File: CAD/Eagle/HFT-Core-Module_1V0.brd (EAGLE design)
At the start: 96.5 x 96.5 mm, 392 parts, among them Q0521 ABS07-32.768KHZ, Q0811 ABM03B-32.000MHZ, Q0911 ABM3B-16MHZ-10-R50-1-U, T1201 MMBT2222, T1202 MMBT2222, T1203 MMBT2222, U0111 STM32L4Z_144PIN_SMPS, U0431 PAM2305AAB120, U0601 LM4120IM5-3.0, U0611 MAX5217, U0631 CFPT-141-20MHZ, U0641 OPA354, U0701 Si5338, U0801 SX1276, U0901 AX5243, U0911 PE4259, U0921 PE4259, U0991 PE4259, U1011 MAX5136AGTG+, U1101 MCP3911A0-E-SS, U1121 OPA354, U1131 OPA354, U1141 OPA354, U1201 NHD-C0220BIZ_2X20CHARS, U1301 MPU-9250, U1311 MS5607-02BA03, U1321 SHT31-DIS, U1401 SOLARPANEL_3V3_5MA1_25MM_X_20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, U1402 SPV1040T, U1501 TS5A23166, U1601 PAM2305AAB330, U1701 TS5A23166, U1801 TS5A23166, U1901 TS5A23166, X1261 TTE_EN11-HSM, X2101 SMA_SMT_AMPHENOL-901-143, X2111 SMA_SMT_AMPHENOL-901-143, X2201 CUI SJ1-3535NS, X2211 CUI SJ1-3535NS, X2311 2X20/90_1MM27_HARWIN_M50-3202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, X2312 2X20/90_1MM27_HARWIN_M50-3202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, X2321 2X20/90_1MM27_HARWIN_M50-3202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, X2322 2X20/90_1MM27_HARWIN_M50-3202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, X2331 2X20/90_1MM27_HARWIN_M50-3202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, X2332 2X20/90_1MM27_HARWIN_M50-3202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

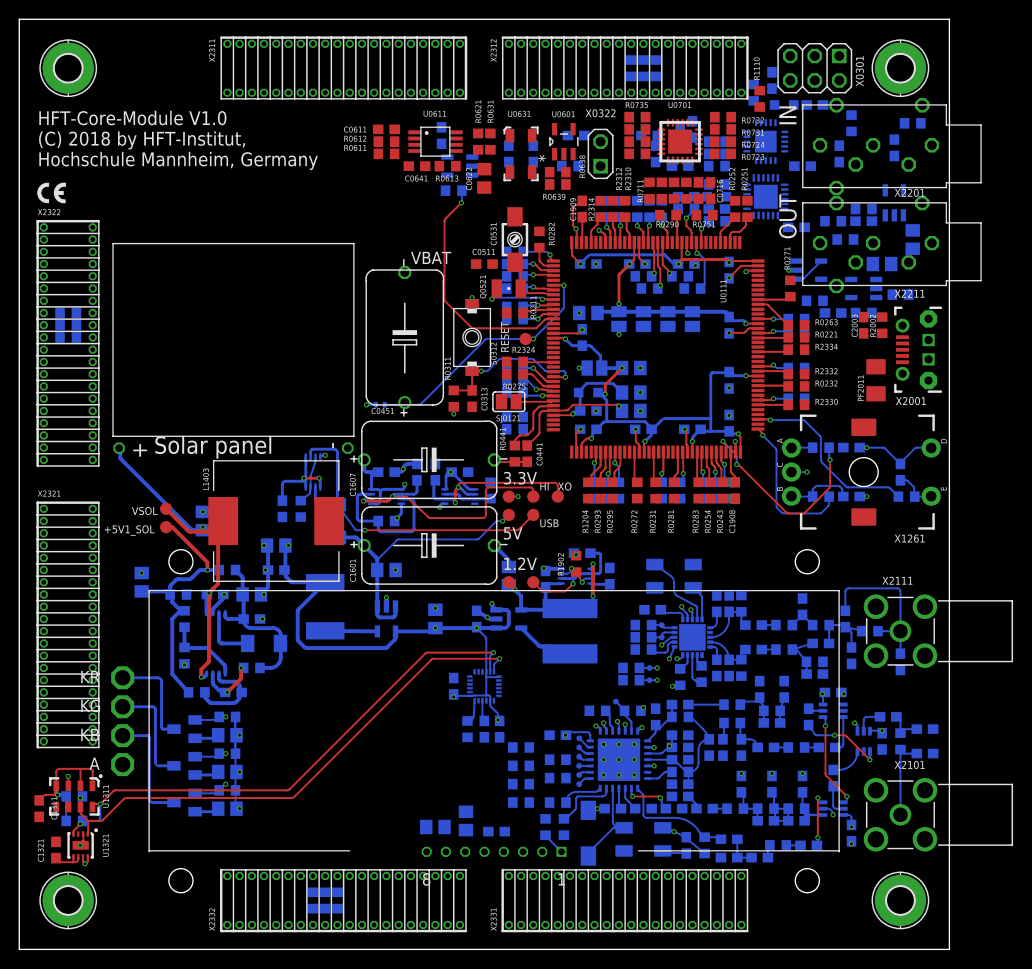
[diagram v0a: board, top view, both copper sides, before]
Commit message: HW_1V0 - many more lines added
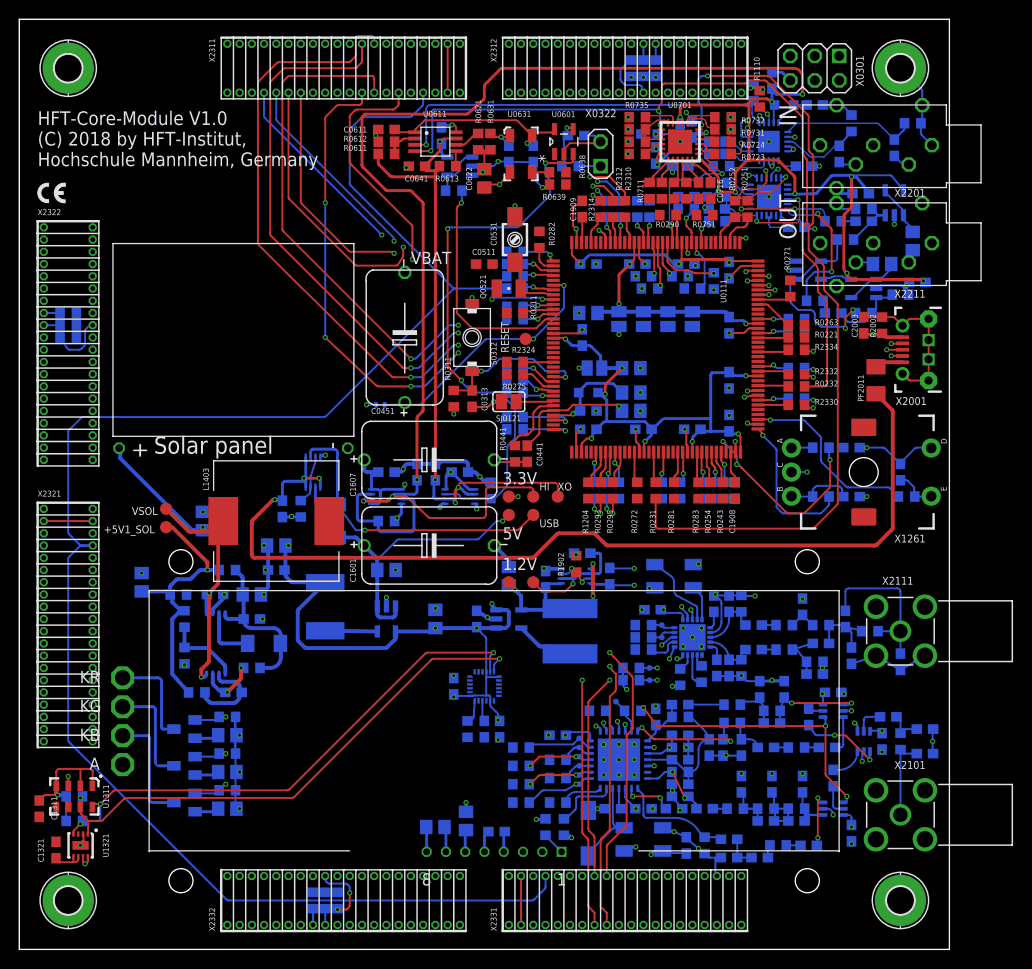
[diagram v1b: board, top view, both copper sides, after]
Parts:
- added C1128, C1129: 100nF, df4iah_rcl:C0603
- moved R0285 9.21 mm to (72.1, 69.4), turned to 270 degrees
- moved R1109 0.48 mm to (72.9, 81.3)
- moved C1002 0.32 mm to (72.1, 35.9)
- moved U1011 0.32 mm to (77.8, 78.1)
- moved U1101 0.32 mm to (77.8, 83.8)
- moved R1114 0.22 mm to (72.5, 79.5)
- moved C0701 0.16 mm to (66.0, 82.4)
- moved C0705 0.16 mm to (65.4, 84.6)
- moved C1103 0.16 mm to (81.4, 81.3)
- moved C1132 0.16 mm to (92.7, 73.5)
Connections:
- net CLK0N renamed CLK0_N
- net CLK0P renamed CLK0_P
- net CLK1N renamed CLK1_N
- net CLK1P renamed CLK1_P
- net CLK2N renamed CLK2_N
- net CLK2P renamed CLK2_P
- net PA11 renamed PA_USB_N
- net PA12 renamed PA_USB_P
- net +3V3_HICUR: now also C1128.1, C1129.1
- net GND: now also C1128.2, C1129.2
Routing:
- net +3V3_HICUR: track 27.0 -> 222.4 mm, vias 2 -> 16
- net MCU_WAKEUP: track 0.00 -> 176.3 mm
- net GND: track 97.6 -> 246.2 mm, vias 68 -> 129
- net MCU_I2C4_SCL: track 55.1 -> 171.8 mm, vias 3 -> 6
- net CLK0_N: track 0.00 -> 100.1 mm, vias 0 -> 1
- net CLK0_P: track 0.00 -> 94.5 mm, vias 0 -> 1
- net VDDUSB: track 10.1 -> 101.2 mm, vias 2 -> 3
- net UART1_CTS_IN: track 0.00 -> 82.3 mm, vias 0 -> 3
- net MCU_I2C4_SDA: track 55.5 -> 137.5 mm, vias 2 -> 5
- net UART1_RX_IN: track 0.00 -> 81.2 mm, vias 0 -> 3
- net UART1_TX_OUT: track 0.00 -> 75.7 mm, vias 0 -> 5
- net CLK1_N: track 0.00 -> 75.1 mm, vias 0 -> 1
- net UART1_RTS_OUT: track 0.00 -> 73.0 mm, vias 0 -> 3
- net CLK1_P: track 0.00 -> 70.0 mm, vias 0 -> 1
- net EVT_S: track 0.00 -> 65.6 mm, vias 0 -> 1
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
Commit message: HW_1V0 - it is getting more delicate now
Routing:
- net +5V0: track 44.5 -> 251.1 mm, vias 1 -> 3
- net PD12: track 39.9 -> 178.0 mm, vias 2 -> 7
- net PD11: track 41.0 -> 177.4 mm, vias 2 -> 7
- net PB13: track 43.0 -> 176.7 mm, vias 2 -> 6
- net I2S_MCLK_OUT: track 0.00 -> 133.0 mm, vias 0 -> 4
- net I2S_FS_OUT: track 0.00 -> 132.6 mm, vias 0 -> 4
- net MCU_SPI1_MISO: track 0.00 -> 130.6 mm, vias 0 -> 4
- net MCU_SPI1_MOSI: track 0.00 -> 128.6 mm, vias 0 -> 4
- net MCU_SPI1_SCK: track 0.00 -> 126.0 mm, vias 0 -> 3
- net I2S_SCK_OUT: track 0.00 -> 125.5 mm, vias 0 -> 4
- net MCU_I2C4_SDA: track 137.5 -> 228.3 mm, vias 5 -> 9
- net EVT_W: track 0.00 -> 59.3 mm, vias 0 -> 2
- net MCU_VDD12: track 18.5 -> 75.6 mm, vias 1 -> 2
- net MCU_I2C4_SCL: track 171.8 -> 228.6 mm, vias 6 -> 8
- net MCU_I2C2_SDA: track 0.00 -> 53.1 mm, vias 0 -> 1
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
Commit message: HW_1V0 - routing first iteration done
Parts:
- added FM1, FM2, FM3: (no value), df4iah_fiducial:FIDUCIAL_MARK_1MM
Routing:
- net I2S_SD_OUT: track 11.8 -> 215.7 mm, vias 0 -> 4
- net LED_R_B: track 3.32 -> 102.9 mm, vias 1 -> 2
- net MCU_I2C3_SDA: track 0.00 -> 99.2 mm, vias 0 -> 4
- net MCU_I2C3_SCL: track 0.00 -> 98.4 mm, vias 0 -> 4
- net UART2_RX_IN: track 0.00 -> 94.0 mm, vias 0 -> 1
- net I2S_SCK_OUT: track 125.5 -> 216.2 mm, vias 4 -> 6
- net PW03: track 0.00 -> 90.2 mm, vias 0 -> 4
- net I2S_FS_OUT: track 132.6 -> 221.7 mm, vias 4 -> 5
- net I2S_MCLK_OUT: track 133.0 -> 221.3 mm, vias 4 -> 7
- net PW02: track 0.00 -> 87.2 mm, vias 0 -> 4
- net UART2_RTS_OUT: track 0.00 -> 84.8 mm, vias 0 -> 2
- net PW01: track 0.00 -> 84.3 mm, vias 0 -> 4
- net MCU_SPI1_MOSI: track 128.6 -> 212.9 mm, vias 4 -> 7
- net MCU_SPI1_MISO: track 130.6 -> 213.2 mm, vias 4 -> 8
- net MCU_SPI1_SCK: track 126.0 -> 208.6 mm, vias 3 -> 6
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
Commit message: HW_1V0 - ERC: some missing signals at the MCU found
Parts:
- X2001: value (none) -> MOLEX 105017-0001
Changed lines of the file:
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@@
 <attribute name="VALUE" x="37.465" y="45.339" size="0.6096" layer="27" font="vector" ratio="10"/>
 </element>
-<element name="X2001" library="df4iah_connector" package="USB-B-MICRO-SMD_MOLEX-105017-0001" value="" x="95.8088" y="62.23" locked="yes" smashed="yes" rot="R90">
+<element name="X2001" library="df4iah_connector" package="USB-B-MICRO-SMD_MOLEX-105017-0001" value="MOLEX 105017-0001" x="95.8088" y="62.23" locked="yes" smashed="yes" rot="R90">
 <attribute name="NAME" x="90.932" y="56.4896" size="0.8128" layer="25" font="vector" ratio="15"/>
 <attribute name="VALUE" x="94.5769" y="67.9196" size="0.6096" layer="27" font="vector" ratio="20" rot="R180" align="top-left"/>

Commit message: HW_1V0 - TIM5 capture channels 1-3 added to the North, West and the South
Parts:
- added R2318, R2328, R2338: 47R, rcl:R0603
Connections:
- new net CAP_N: R2318.2, X2311.31
- new net CAP_S: R2338.2, X2331.31
- new net CAP_W: R2328.2, X2321.31
- net GND: no longer X2311.31, X2321.31, X2331.31
- net PF6: now also R2318.1
- net PF7: now also R2328.1
- net PF8: now also R2338.1
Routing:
- net PF7: track 0.00 -> 72.9 mm, vias 0 -> 2
- net PF8: track 0.00 -> 61.4 mm, vias 0 -> 4
- net PF6: track 0.00 -> 41.7 mm, vias 0 -> 2
- net UART2_CTS_IN: track 66.2 -> 63.9 mm
- net CAP_S: track 0.00 -> 1.69 mm
- net CAP_W: track 0.00 -> 1.54 mm
- net CAP_N: track 0.00 -> 1.44 mm

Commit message: HW_1V0 - work of the day
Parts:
- added R1411: 1kR, rcl:R0603
- added R1412: 100kR, rcl:R0603
- moved R0261 6.02 mm to (78.1, 73.7), flipped to the top, turned to 90 degrees
- renumbered U1011 to U1111
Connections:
- net CAP_N renamed TIMCAP_N
- net CAP_S renamed TIMCAP_S
- net CAP_W renamed TIMCAP_W
- net PA3: now also R1411.2
- net PF9: now also R1412.1
- net SPV_LX: now also R1412.2
- net VSOL: now also R1411.1
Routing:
- net MCU_SPI3_SCK: track 8.33 -> 115.7 mm, vias 4 -> 6
- net AX_16MHZ: track 0.84 -> 99.9 mm, vias 1 -> 6
- net MCU_SPI3_MOSI: track 9.80 -> 107.2 mm, vias 4 -> 6
- net PC11: track 0.50 -> 97.0 mm, vias 1 -> 6
- net PE7: track 0.00 -> 58.5 mm, vias 0 -> 3
- net PG1: track 0.00 -> 53.6 mm, vias 0 -> 3
- net PA3: track 0.00 -> 40.6 mm, vias 0 -> 2
- net PG3: track 0.00 -> 37.1 mm, vias 0 -> 2
- net PH0: track 0.00 -> 36.7 mm, vias 0 -> 3
- net PF9: track 0.00 -> 36.1 mm, vias 0 -> 2
- net MCU_MCO: track 0.00 -> 25.5 mm, vias 0 -> 2
- net SPV_LX: track 5.92 -> 30.4 mm, vias 0 -> 1
- net PD1: track 0.00 -> 23.2 mm, vias 0 -> 2
- net PC8: track 0.00 -> 22.8 mm, vias 0 -> 2
- net PD2: track 0.00 -> 18.4 mm, vias 0 -> 2
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
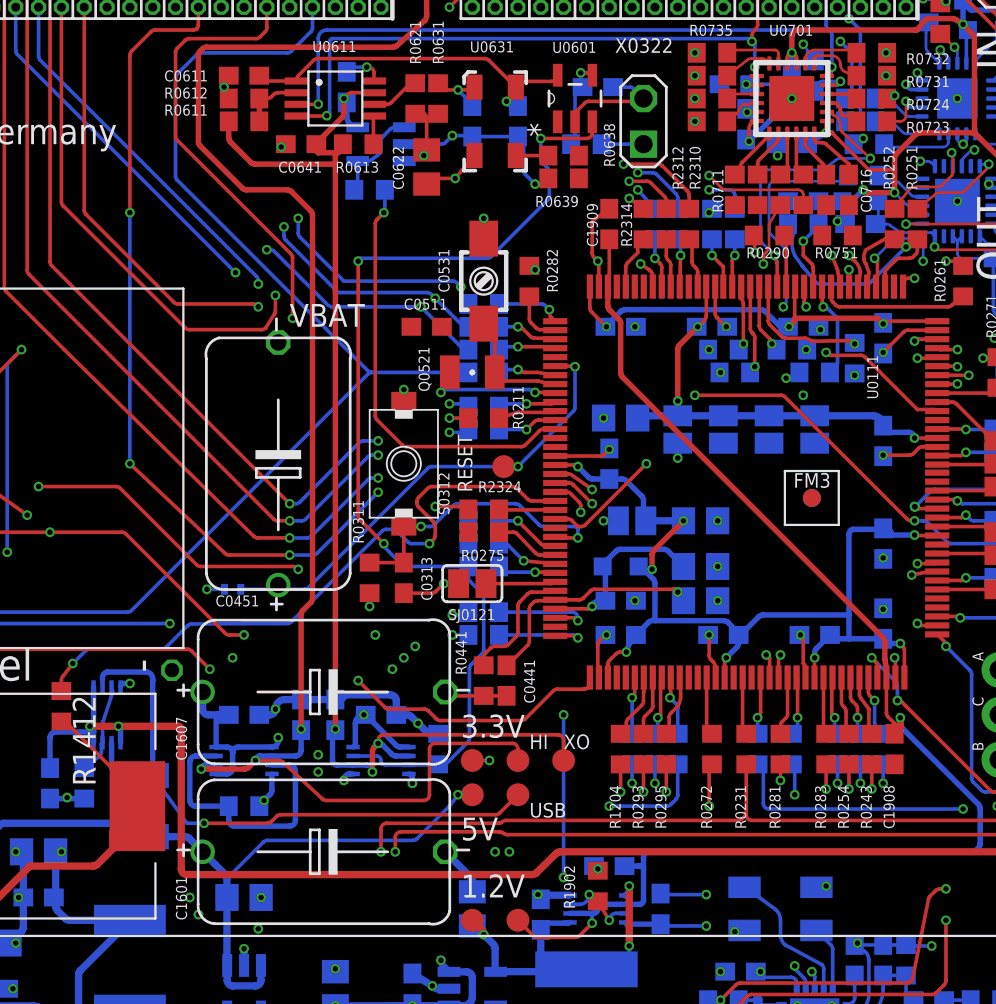
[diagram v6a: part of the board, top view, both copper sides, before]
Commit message: HW_1V0 - enable lines to the switchers routed
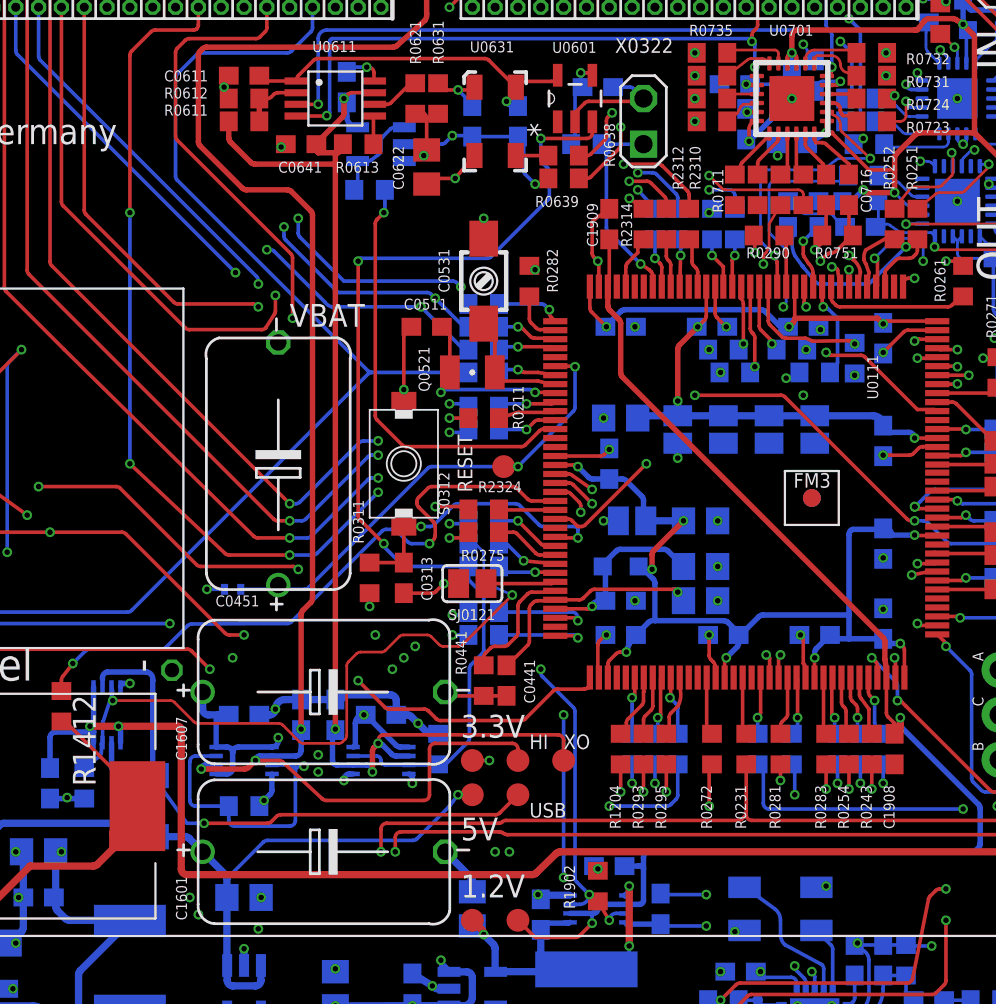
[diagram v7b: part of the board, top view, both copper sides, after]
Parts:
- moved C1112 0.16 mm to (72.4, 76.7)
- moved R0262 0.16 mm to (69.2, 76.7)
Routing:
- net MCU_OUT_VUSB_EN: track 5.07 -> 39.1 mm, vias 0 -> 2
- net MCU_OUT_VDD12_EN: track 4.21 -> 29.5 mm, vias 2 -> 4
- net 20MHZ_XOP: track 0.00 -> 25.0 mm, vias 0 -> 2
- net 20MHZ_XON: track 0.00 -> 23.6 mm, vias 0 -> 2
- net MCU_OUT_HICUR_EN: track 15.0 -> 33.7 mm, vias 0 -> 2
- net PH3_BOOT0: track 3.90 -> 11.4 mm
- net GND: track 251.0 -> 257.9 mm, vias 130 -> 129
- net PC15_MCU_OSC32_OUT: track 7.71 -> 10.4 mm
- net I2S_MCLK_OUT: track 221.7 -> 222.8 mm
- net PC11: track 97.0 -> 97.7 mm

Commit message: HW_1V0 - now everything routed?
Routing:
- net PD8: track 0.00 -> 95.1 mm, vias 0 -> 4
- net PG2: track 12.4 -> 103.8 mm, vias 3 -> 5
- net PF13: track 0.00 -> 52.1 mm, vias 0 -> 3
- net PG3: track 37.1 -> 80.9 mm, vias 2 -> 3
- net MCU_VDD: track 79.1 -> 87.5 mm
- net PC11: track 97.7 -> 105.3 mm
